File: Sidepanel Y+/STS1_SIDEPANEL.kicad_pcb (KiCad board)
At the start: 2 copper layers, 82.8 x 100 mm, 49 parts, among them IC1 TMP112AQDRLRQ1, J1 Conn_02x04_Odd_Even, J2 Conn_02x02_Odd_Even, U1 GUVA-C32SM

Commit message: Review Ready for V2.0
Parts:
- CUR1, CUR2: footprint SamacSys:SOIC127P600X175-8N -> Package_SO:SOIC-8_3.9x4.9mm_P1.27mm
- DOUT1, DOUT2: footprint SamacSys:STMITE -> Diode_SMD:D_0603_1608Metric
- IC1: footprint SamacSys:SOTFL50P160X60-6N -> Package_TO_SOT_SMD:SOT-563
- J1: footprint SamacSys:M808280842 -> STS_Connector:M808280842
- J2: footprint USER_Passiv:M80-8280442 -> STS_Connector:M808280442
- L_IN1, L_IN2: footprint SamacSys:INDPM5650X530N -> Inductor_SMD:L_0603_1608Metric
- MPPT1, MPPT2: footprint SamacSys:SOP65P640X120-8N -> Package_SO:TSSOP-8_4.4x3mm_P0.65mm
- SC1, SC2: footprint USER_Activ:3G30A_40x80 -> STS_Connector:3G30A_40x80
- U1: footprint USER_Optic:OLGA 2mm x 2,3mm -> Package_SO:SO-4_4.4x3.6mm_P2.54mm
- moved U1 72.7 mm to (87.0, 48.5), turned to 90 degrees
- moved J2 56.7 mm to (105.2, 61.1)
- moved J1 31.4 mm to (117.6, 61.1), turned to 180 degrees
- moved SC1 2.00 mm to (125.0, 68.5), turned to 0 degrees
- moved SC2 2.00 mm to (125.0, 110.5), turned to 180 degrees
- moved C2 1.17 mm to (142.8, 86.3)
- moved RIC1 0.94 mm to (141.8, 93.9)
- moved RIC2 0.94 mm to (143.8, 93.9)
- moved RU1 0.94 mm to (148.0, 93.9)
- moved RU2 0.94 mm to (146.0, 93.9)
- moved C_CUR11 0.89 mm to (123.9, 83.0)
- moved C_CUR21 0.89 mm to (125.6, 83.0)
- moved C1 0.42 mm to (147.0, 86.3)
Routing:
- net /SC2_V+: track 27.7 -> 134.3 mm, vias 7 -> 2
- net /Sensors/VBAT: track 2.06 -> 105.4 mm
- net /SDA: track 18.5 -> 120.3 mm, vias 1 -> 2
- net /SCL: track 17.8 -> 95.9 mm, vias 1 -> 2
- net /+3V3: track 33.2 -> 94.3 mm
- net /SC1_V+: track 14.6 -> 62.8 mm, vias 8 -> 2
- net /MPPT1: track 118.6 -> 81.6 mm, vias 4 -> 5
- net /SC2_I+: track 31.6 -> 57.3 mm
- net /MPPT2: track 93.2 -> 117.7 mm
- net /SC1_I+: track 24.3 -> 29.1 mm
- net GND: track 10.9 -> 15.7 mm, vias 264 -> 243
- net /SolarMPPT/MPPT1_IN: track 6.57 -> 8.58 mm
- removed copper zone on B.Cu, net /SC1_V+
- removed copper zone on F.Cu, net /SC1_V+
- removed copper zone on B.Cu, net /SC2_V+
- removed copper zone on F.Cu, net /SC2_V+
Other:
- outline, holes or cut-outs redrawn

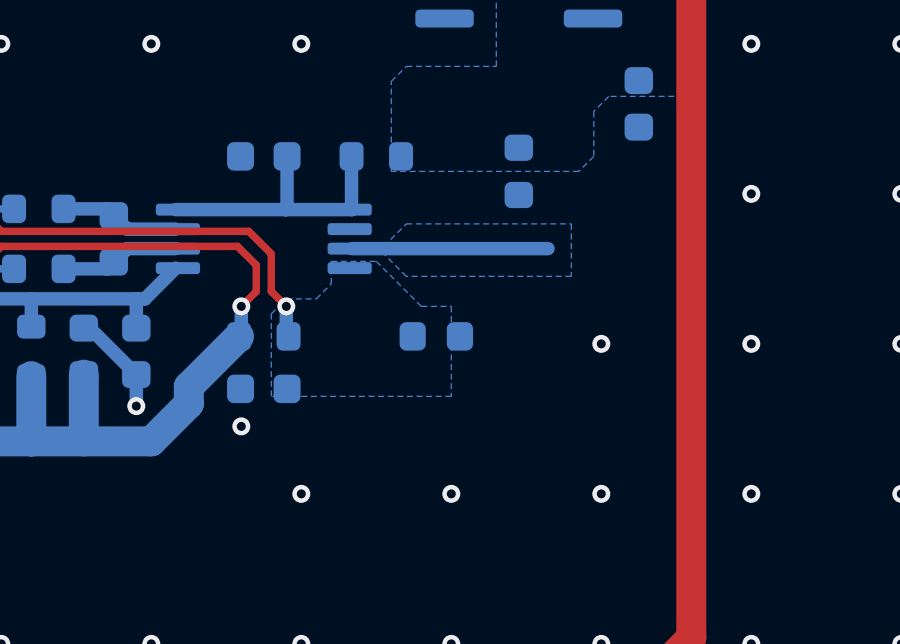
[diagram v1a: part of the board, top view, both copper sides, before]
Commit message: Paar Fehler behoben, Z+ no MOSFET
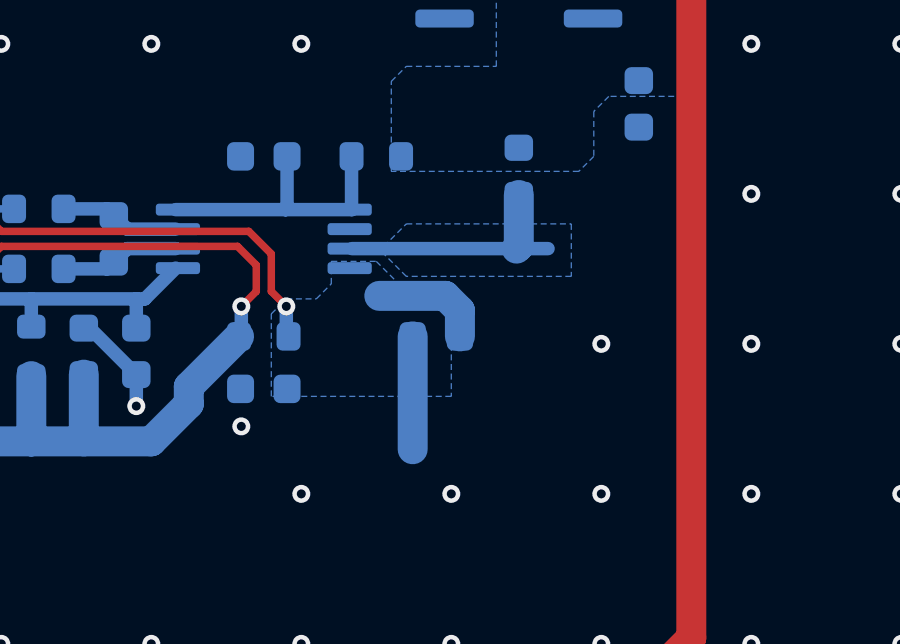
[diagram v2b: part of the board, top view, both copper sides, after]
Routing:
- net GND: track 15.7 -> 19.5 mm
- net /SolarMPPT/MPPT2_OUT: track 14.5 -> 18.3 mm
- net /SolarMPPT/MPPT2_IN: track 6.57 -> 8.39 mm
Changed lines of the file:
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@@
   (segment (start 132.05 69.775) (end 130.5 68.225) (width 0.45) (layer "B.Cu") (net 1))
   (segment (start 117.75 108.975) (end 117.95 108.975) (width 0.45) (layer "B.Cu") (net 1))
+  (segment (start 128.7125 109.25) (end 128.7125 113.0125) (width 1) (layer "B.Cu") (net 1))
   (segment (start 85.73 45.35) (end 88.87952 42.20048) (width 0.2) (layer "F.Cu") (net 2))
   (segment (start 147.8 45.802151) (end 147.8 81.9) (width 0.2) (layer "F.Cu") (net 2))
@@
   (via (at 124.5 108.25) (size 0.6) (drill 0.3) (layers "F.Cu" "B.Cu") (free) (net 24))
   (via (at 114.25 105) (size 0.6) (drill 0.3) (layers "F.Cu" "B.Cu") (net 24))
+  (segment (start 130.2875 109.25) (end 130.2875 108.3875) (width 1) (layer "B.Cu") (net 24))
   (segment (start 124.5 108.25) (end 124.5 109.175) (width 0.45) (layer "B.Cu") (net 24))
   (segment (start 124.5 109.175) (end 124.575 109.25) (width 0.45) (layer "B.Cu") (net 24))
+  (segment (start 129.8 107.9) (end 127.6 107.9) (width 1) (layer "B.Cu") (net 24))
+  (segment (start 130.2875 108.3875) (end 129.8 107.9) (width 1) (layer "B.Cu") (net 24))
   (segment (start 115.425 105) (end 114.25 105) (width 0.25) (layer "B.Cu") (net 24))
   (segment (start 118.275 72.425) (end 116.775 72.425) (width 0.45) (layer "B.Cu") (net 27))
@@
   (segment (start 117.775 72.425) (end 117.75 72.4) (width 0.3) (layer "B.Cu") (net 27))
   (segment (start 117.75 72.95) (end 117.75 74.2125) (width 0.45) (layer "B.Cu") (net 27))
-  (segment (start 126.688 106.325) (end 133.225 106.325) (width 0.45) (layer "B.Cu") (net 28))
+  (segment (start 132.25 104.5375) (end 132.25 106.25) (width 1) (layer "B.Cu") (net 28))
   (segment (start 132.225 106.325) (end 132.25 106.35) (width 0.3) (layer "B.Cu") (net 28))
+  (segment (start 126.688 106.325) (end 132.175 106.325) (width 0.45) (layer "B.Cu") (net 28))
+  (segment (start 132.25 106.25) (end 132.175 106.325) (width 1) (layer "B.Cu") (net 28))
+  (segment (start 132.175 106.325) (end 133.225 106.325) (width 0.45) (layer "B.Cu") (net 28))
   (zone (net 1) (net_name "GND") (layers F&B.Cu) (hatch edge 0.508)
     (connect_pads (clearance 0.2))

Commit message: Further fixes, still some open
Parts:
- SC1, SC2: footprint STS_Connector:3G30A_40x80 -> STS_Solarcells:3G30A_40x80
- moved C1 52.3 mm to (106.8, 52.9), turned to -90 degrees
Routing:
- net /Sensors/VBAT: track 105.4 -> 28.0 mm
- net /SCL: track 95.9 -> 131.3 mm
- net /SC1_I+: track 29.1 -> 49.2 mm
- net /MPPT2: track 117.7 -> 100.9 mm, vias 4 -> 0
- net /MPPT1: track 81.6 -> 75.1 mm, vias 5 -> 3
- net /SolarMPPT/MPPT1_OUT: track 14.5 -> 20.1 mm
- net /SC2_V+: track 134.3 -> 138.9 mm, vias 2 -> 1
- net /SDA: track 120.3 -> 124.5 mm
- net /SolarMPPT/MPPT2_OUT: track 18.3 -> 22.5 mm
- net /SC1_V+: track 62.8 -> 66.3 mm, vias 2 -> 1
